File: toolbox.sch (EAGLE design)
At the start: 56 parts, among them IC1 PIC18F4XK22PT, IC2 7805TV

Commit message: added board
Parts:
- removed IC2: 7805TV, linear:7805TV
- removed LINK: (no value), con-lstb:MA06-2
- removed POWER_LEDS, SENSORS, SENSORS_GND: (no value), con-lstb:MA05-1
- removed RASPI_ALIM, RASPI_ALIM1: (no value), con-lstb:MA03-1
- removed XB1: XBEE, maxstream:XBEE
- added AX12, USB: (no value), con-amp:SMDTOP-4
- added C4: 22uF, rcl:CPOL-USE2-5
- added C5: 0.47uF, rcl:CPOL-USE2-5
- added C6, C7, C8, C9: 100n, rcl:C-USC0805
- added D6, D7: (no value), diode:DIODE-SOD523
- added IC3: 78L05SMD, linear:78L05SMD
- added R30, R31, R33, R35: 10k, rcl:R-US_M0805
- added R32: 1k, rcl:R-US_M0805
- added R34: 22k, rcl:R-US_M0805
- added R38: 360, rcl:R-US_M0805
- added RPI, RPI2: (no value), con-amp:SMDTOP-6
- added SV1: (no value), con-lstb:MA05-2
- added T1: BC847, transistor:BC847
- added U$1: REGUL_PTH, regul_pth:REGUL_PTH
- added U2: AD654JRZ, AD654:AD654JRZ
- added U3: ADUM7441ARQZ, ADUM7441:ADUM7441ARQZ
- BUTTONS: device con-lstb:MA03-1 -> con-amp:SMDTOP-4
- C1: value 0.47uF -> 100uF; device rcl:CPOL-USE2-5 -> rcl:CPOL-USE2,5-6E
- C2: value 22uF -> 100uF; device rcl:CPOL-USE2-5 -> rcl:CPOL-USE2,5-6E
- COLLISION: device con-lstb:MA08-1 -> con-amp:SMDTOP-10
- LEDS: device con-lstb:MA05-1 -> con-amp:SMDTOP-10
- R28: value 1k -> 2.2k
- R29: value 1k -> 4.7k
- renumbered X1 to LOGIC, X2 to MOTORS
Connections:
- new net N$51: R30.2, T1.B
- new net N$52: AX12-3.1, D6.A, T1.E
- new net N$53: D6.C, R30.1, R32.2
- new net N$54: IC1.RC7/RX1/DT1/AN19, U3.VOC
- new net N$55: R31.2, T1.C, U3.VIC
- new net N$56: IC1.RC6/TX1/CK1/AN18, U3.VID
- new net N$58: R38.1, U$1.VADJ
- new net N$59: D7.A, R32.1, U3.VOD
- new net N$61: AX12-2.1, C5.+, IC3G$1.VIN, MOTORS-1.SK, R34.2, U2.+VS
- new net N$62: C8.2, U2.CT_2
- new net N$63: R33.1, U2.FOUT, U3.VIB
- new net N$65: R29.2, U2.RT
- new net N$67: AX12-4.1, C4.-, C5.-, IC3G$1.GND@1, IC3G$1.GND@2, IC3G$1.GND@3, IC3G$1.GND@4, MOTORS-2.SK, R29.1, R35.1, U2.-VS, U2.LOGIC_COM, U3.GND1, U3.GND1*
- new net N$68: C4.+, D7.C, IC3G$1.VOUT, R31.1, R33.2, U3.VDD1A, U3.VDD1B
- net GND: now also C6.2, C7.2, C9.2, COLLISION-10.1, COLLISION-9.1, LEDS-1.1, LEDS-2.1, R38.2, RPI-3.1, RPI2-3.1, SV1.10, SV1.2, SV1.4, SV1.6, SV1.8, U$1.GND, U3.GND2, U3.GND2_2, USB-1.1, USB-4.1; no longer COLLISION.8, IC2.GND, LEDS.5, LINK.5, LINK.6, POWER_LEDS.5, RASPI_ALIM.1, RASPI_ALIM.3, RASPI_ALIM1.1, RASPI_ALIM1.2, RASPI_ALIM1.3, SENSORS_GND.1, SENSORS_GND.2, SENSORS_GND.3, SENSORS_GND.4, SENSORS_GND.5, XB1.GND
- net N$10: now also LEDS-3.1; no longer LEDS.1
- net N$11: now also SV1.9; no longer SENSORS.5
- net N$12: now also SV1.7; no longer SENSORS.4
- net N$13: now also SV1.5; no longer SENSORS.3
- net N$14: now also SV1.3; no longer SENSORS.2
- net N$15: now also SV1.1; no longer SENSORS.1
- net N$24: now also BUTTONS-4.1; no longer BUTTONS.1
- net N$25: now also BUTTONS-2.1; no longer BUTTONS.3
- net N$26: now also BUTTONS-3.1; no longer BUTTONS.2
- net N$3: now also C9.1, R28.2
- net N$31: now also LEDS-10.1; no longer POWER_LEDS.4
- net N$32: now also LEDS-9.1; no longer POWER_LEDS.3
- net N$33: now also LEDS-8.1; no longer POWER_LEDS.2
- net N$34: now also LEDS-7.1; no longer POWER_LEDS.1
- net N$35: now also COLLISION-1.1, COLLISION-2.1, U$1.VI; no longer COLLISION.1, IC2.VI
- net N$36: now also DEBUG.2; no longer R29.2
- net N$37: now also U$1.VO, USB-2.1, USB-3.1; no longer IC2.VO, RASPI_ALIM.2
- net N$38: now also DEBUG.3; no longer R28.2
- net N$4: now also LEDS-6.1; no longer LEDS.4
- net N$41: now also COLLISION-4.1; no longer COLLISION.3
- net N$42: now also COLLISION-5.1; no longer COLLISION.4
- net N$43: now also COLLISION-6.1; no longer COLLISION.5
- net N$44: now also COLLISION-7.1; no longer COLLISION.6
- net N$45: now also COLLISION-8.1; no longer COLLISION.7
- net N$49: now also R34.1, R35.2, U2.+VIN; no longer DEBUG.2, R28.1, XB1.DIN/!CONFIG
- net N$5: now also LEDS-5.1; no longer LEDS.3
- net N$50: now also C8.1, U2.CT; no longer DEBUG.3, XB1.DOUT
- net N$6: now also LEDS-4.1; no longer LEDS.2
- net N$7: now also RPI-4.1, RPI2-4.1; no longer LINK.7, LINK.8
- net N$8: now also RPI-5.1, RPI2-5.1; no longer LINK.10, LINK.9
- net N$9: now also RPI-6.1, RPI2-6.1; no longer LINK.11, LINK.12
- net VCC: now also BUTTONS-1.1, C6.1, C7.1, R28.1, RPI-2.1, RPI2-2.1, U3.VDD2A, U3.VDD2B; no longer LINK.3, LINK.4, XB1.VCC
- net VDD: now also COLLISION-3.1, RPI-1.1, RPI2-1.1; no longer COLLISION.2, LINK.1, LINK.2
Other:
- moved on the sheet: DEBUG, R28, R29

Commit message: WIP replaced AX-12 connector with 2x6pin micromatch routed motor side parts, sensor, buttons and LEDs connectors
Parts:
- added AX12-2: (no value), con-amp:SMDTOP-6
- added R36: 22k, rcl:R-US_M0805
- AX12: device con-amp:SMDTOP-4 -> con-amp:SMDTOP-6
- R10, R11, R12, R19, R20, R21, R22, R23, R24, R25, R26, R27: value (none) -> 22k
- renumbered SV1 to SENSORS
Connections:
- new net N$57: IC1.RE2/CCP5/AN7, U3.VOB
- net N$27: now also R15.2; no longer R13.2
- net N$29: now also IC1.RC0/P2B/T3CKI/T3G/T1CKI/SOSCO, R16.2; no longer IC1.RE2/CCP5/AN7, R15.2
- net N$30: now also R13.2; no longer R16.2
- net N$39: now also IC1.RA0/C12IN0-/AN0; no longer IC1.RA1/C12IN1-/AN1
- net N$44: no longer R22.1
- net N$45: now also R22.1, R36.2
- net N$46: now also PWM.4; no longer PWM.8
- net N$47: now also PWM.8; no longer PWM.2
- net N$48: now also PWM.2; no longer PWM.4
- net N$52: now also AX12-2-3.1, AX12-2-4.1, AX12-4.1
- net N$61: now also AX12-1.1, AX12-2-1.1, AX12-2-2.1
- net N$67: now also AX12-2-5.1, AX12-2-6.1, AX12-5.1, AX12-6.1, U3.VIA; no longer AX12-4.1
- net VCC: now also R36.1
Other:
- moved on the sheet: AX12-1, AX12-2, AX12-3, AX12-4, R22, R34, R35

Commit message: WIP finished routing the board Removed useless datasheet
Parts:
- added C10, C11: 100n, rcl:C-USC0805
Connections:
- net GND: now also C10.2
- net N$67: now also C11.2
- net N$68: now also C11.1
- net VCC: now also C10.1
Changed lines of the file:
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@@
 <grid distance="0.05" unitdist="inch" unit="inch" style="lines" multiple="1" display="no" altdistance="0.01" altunitdist="inch" altunit="inch"/>
 <layers>
-<layer number="1" name="Top" color="4" fill="1" visible="yes" active="no"/>
-<layer number="16" name="Bottom" color="1" fill="1" visible="yes" active="no"/>
-<layer number="17" name="Pads" color="2" fill="1" visible="yes" active="no"/>
-<layer number="18" name="Vias" color="2" fill="1" visible="yes" active="no"/>
-<layer number="19" name="Unrouted" color="6" fill="1" visible="yes" active="no"/>
-<layer number="20" name="Dimension" color="15" fill="1" visible="yes" active="no"/>
-<layer number="21" name="tPlace" color="7" fill="1" visible="yes" active="no"/>
-<layer number="22" name="bPlace" color="7" fill="1" visible="yes" active="no"/>
-<layer number="23" name="tOrigins" color="15" fill="1" visible="yes" active="no"/>
-<layer number="24" name="bOrigins" color="15" fill="1" visible="yes" active="no"/>
-<layer number="25" name="tNames" color="7" fill="1" visible="yes" active="no"/>
-<layer number="26" name="bNames" color="7" fill="1" visible="yes" active="no"/>
-<layer number="27" name="tValues" color="7" fill="1" visible="yes" active="no"/>
-<layer number="28" name="bValues" color="7" fill="1" visible="yes" active="no"/>
+<layer number="1" name="Top" color="4" fill="1" visible="no" active="no"/>
+<layer number="16" name="Bottom" color="1" fill="1" visible="no" active="no"/>
+<layer number="17" name="Pads" color="2" fill="1" visible="no" active="no"/>
+<layer number="18" name="Vias" color="2" fill="1" visible="no" active="no"/>
+<layer number="19" name="Unrouted" color="6" fill="1" visible="no" active="no"/>
+<layer number="20" name="Dimension" color="15" fill="1" visible="no" active="no"/>
+<layer number="21" name="tPlace" color="7" fill="1" visible="no" active="no"/>
+<layer number="22" name="bPlace" color="7" fill="1" visible="no" active="no"/>
+<layer number="23" name="tOrigins" color="15" fill="1" visible="no" active="no"/>
+<layer number="24" name="bOrigins" color="15" fill="1" visible="no" active="no"/>
+<layer number="25" name="tNames" color="7" fill="1" visible="no" active="no"/>
+<layer number="26" name="bNames" color="7" fill="1" visible="no" active="no"/>
+<layer number="27" name="tValues" color="7" fill="1" visible="no" active="no"/>
+<layer number="28" name="bValues" color="7" fill="1" visible="no" active="no"/>
 <layer number="29" name="tStop" color="7" fill="3" visible="no" active="no"/>
 <layer number="30" name="bStop" color="7" fill="6" visible="no" active="no"/>
@@
 <layer number="35" name="tGlue" color="7" fill="4" visible="no" active="no"/>
 <layer number="36" name="bGlue" color="7" fill="5" visible="no" active="no"/>
-<layer number="37" name="tTest" color="7" fill="1" visible="yes" active="no"/>
-<layer number="38" name="bTest" color="7" fill="1" visible="yes" active="no"/>
+<layer number="37" name="tTest" color="7" fill="1" visible="no" active="no"/>
+<layer number="38" name="bTest" color="7" fill="1" visible="no" active="no"/>
 <layer number="39" name="tKeepout" color="4" fill="11" visible="no" active="no"/>
 <layer number="40" name="bKeepout" color="1" fill="11" visible="no" active="no"/>
@@
 <layer number="44" name="Drills" color="7" fill="1" visible="no" active="no"/>
 <layer number="45" name="Holes" color="7" fill="1" visible="no" active="no"/>
-<layer number="46" name="Milling" color="3" fill="1" visible="yes" active="no"/>
-<layer number="47" name="Measures" color="7" fill="1" visible="yes" active="no"/>
-<layer number="48" name="Document" color="7" fill="1" visible="yes" active="no"/>
-<layer number="49" name="Reference" color="7" fill="1" visible="yes" active="no"/>
-<layer number="51" name="tDocu" color="7" fill="1" visible="yes" active="no"/>
-<layer number="52" name="bDocu" color="7" fill="1" visible="yes" active="no"/>
+<layer number="46" name="Milling" color="3" fill="1" visible="no" active="no"/>
+<layer number="47" name="Measures" color="7" fill="1" visible="no" active="no"/>
+<layer number="48" name="Document" color="7" fill="1" visible="no" active="no"/>
+<layer number="49" name="Reference" color="7" fill="1" visible="no" active="no"/>
+<layer number="51" name="tDocu" color="7" fill="1" visible="no" active="no"/>
+<layer number="52" name="bDocu" color="7" fill="1" visible="no" active="no"/>
 <layer number="90" name="Modules" color="5" fill="1" visible="yes" active="yes"/>
 <layer number="91" name="Nets" color="2" fill="1" visible="yes" active="yes"/>
@@
 <part name="P+12" library="supply1" deviceset="VCC" device=""/>
 <part name="GND15" library="supply1" deviceset="GND" device=""/>
+<part name="P+13" library="supply1" deviceset="VCC" device=""/>
+<part name="GND16" library="supply1" deviceset="GND" device=""/>
+<part name="C10" library="rcl" deviceset="C-US" device="C0805" value="100n"/>
+<part name="C11" library="rcl" deviceset="C-US" device="C0805" value="100n"/>
 </parts>
 <sheets>
@@
 <instance part="P+12" gate="VCC" x="121.92" y="48.26"/>
 <instance part="GND15" gate="1" x="121.92" y="22.86"/>
+<instance part="P+13" gate="VCC" x="191.77" y="63.5"/>
+<instance part="GND16" gate="1" x="191.77" y="49.53"/>
+<instance part="C10" gate="G$1" x="191.77" y="57.15"/>
+<instance part="C11" gate="G$1" x="209.55" y="38.1"/>
 </instances>
 <busses>
@@
 <pinref part="R36" gate="G$1" pin="1"/>
 <pinref part="P+12" gate="VCC" pin="VCC"/>
+</segment>
+<segment>
+<pinref part="C10" gate="G$1" pin="1"/>
+<pinref part="P+13" gate="VCC" pin="VCC"/>
+<wire x1="191.77" y1="60.96" x2="191.77" y2="59.69" width="0.1524" layer="91"/>
 </segment>
 </net>
@@
 <pinref part="R22" gate="G$1" pin="2"/>
 <pinref part="GND15" gate="1" pin="GND"/>
+</segment>
+<segment>
+<pinref part="GND16" gate="1" pin="GND"/>
+<pinref part="C10" gate="G$1" pin="2"/>
 </segment>
 </net>
@@
 <wire x1="209.55" y1="26.67" x2="209.55" y2="13.97" width="0.1524" layer="91"/>
 <junction x="209.55" y="13.97"/>
+<pinref part="C11" gate="G$1" pin="2"/>
+<wire x1="209.55" y1="26.67" x2="209.55" y2="33.02" width="0.1524" layer="91"/>
+<junction x="209.55" y="26.67"/>
 </segment>
 </net>
@@
 <wire x1="205.74" y1="5.08" x2="205.74" y2="39.37" width="0.1524" layer="91"/>
 <wire x1="205.74" y1="39.37" x2="205.74" y2="54.61" width="0.1524" layer="91"/>
-<wire x1="205.74" y1="54.61" x2="217.17" y2="54.61" width="0.1524" layer="91"/>
+<wire x1="205.74" y1="54.61" x2="209.55" y2="54.61" width="0.1524" layer="91"/>
 <junction x="217.17" y="54.61"/>
+<wire x1="209.55" y1="54.61" x2="217.17" y2="54.61" width="0.1524" layer="91"/>
 <wire x1="200.66" y1="39.37" x2="205.74" y2="39.37" width="0.1524" layer="91"/>
 <junction x="200.66" y="39.37"/>
 <junction x="205.74" y="39.37"/>
-</segment>
-</net>
+<pinref part="C11" gate="G$1" pin="1"/>
+<wire x1="209.55" y1="40.64" x2="209.55" y2="54.61" width="0.1524" layer="91"/>
+<junction x="209.55" y="54.61"/>
+</segment>
+</net>

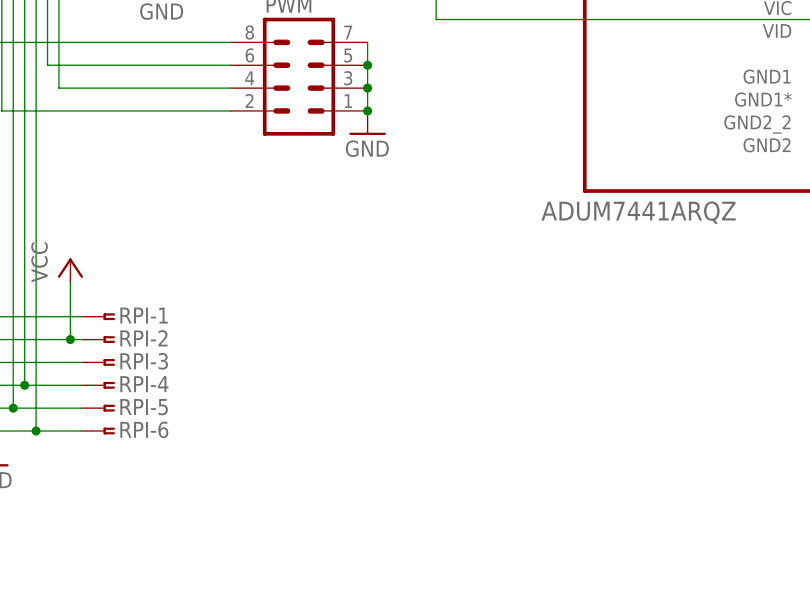
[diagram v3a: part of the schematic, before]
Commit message: moved labels and created ground planes with vias between them
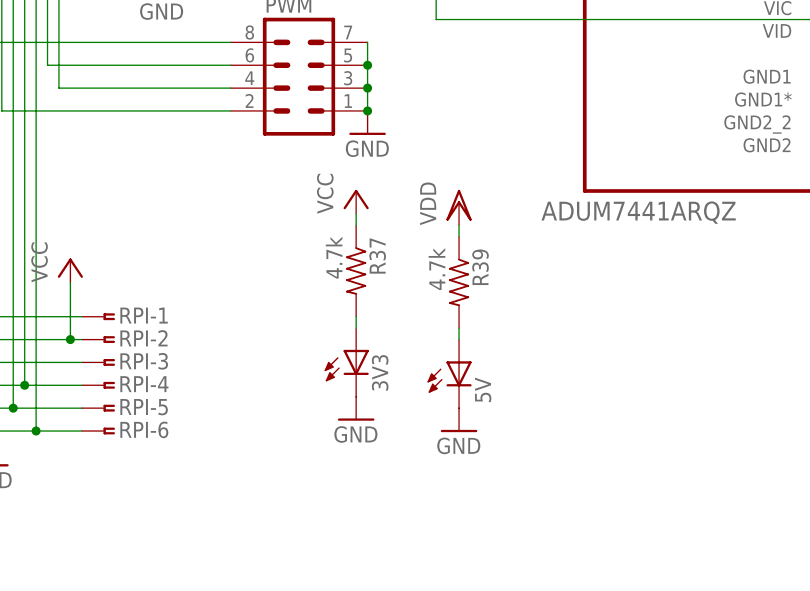
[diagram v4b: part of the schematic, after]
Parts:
- added 3V3, 5V: (no value), adafruit:LEDCHIPLED_0805
- added R37, R39: 4.7k, rcl:R-US_M0805
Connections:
- net N$67 renamed GND_MOTOR
- new net N$60: 3V3.A, R37.2
- new net N$64: 5V.A, R39.2
- net GND: now also 3V3.C, 5V.C
- net VCC: now also R37.1
- net VDD: now also R39.1
